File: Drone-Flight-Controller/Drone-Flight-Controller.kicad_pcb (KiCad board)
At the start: 2 copper layers, 30 x 65 mm, 45 parts, among them J1 Screw_Terminal_01x02, J10 TestPoint, J11 TestPoint, J12 TestPoint, J2 Raspberry_Pi_4, J3 TestPoint, J4 TestPoint, J5 TestPoint, J6 TestPoint, J7 TestPoint, J8 TestPoint, J9 TestPoint, SW1 SW_Omron_B3FS, U1 MCP1700x-180xxMB, U2 LMR51430, U3 ADC101C021CIMK, U4 ICM-20948, U5 BMP280, U6 PCA9531PW

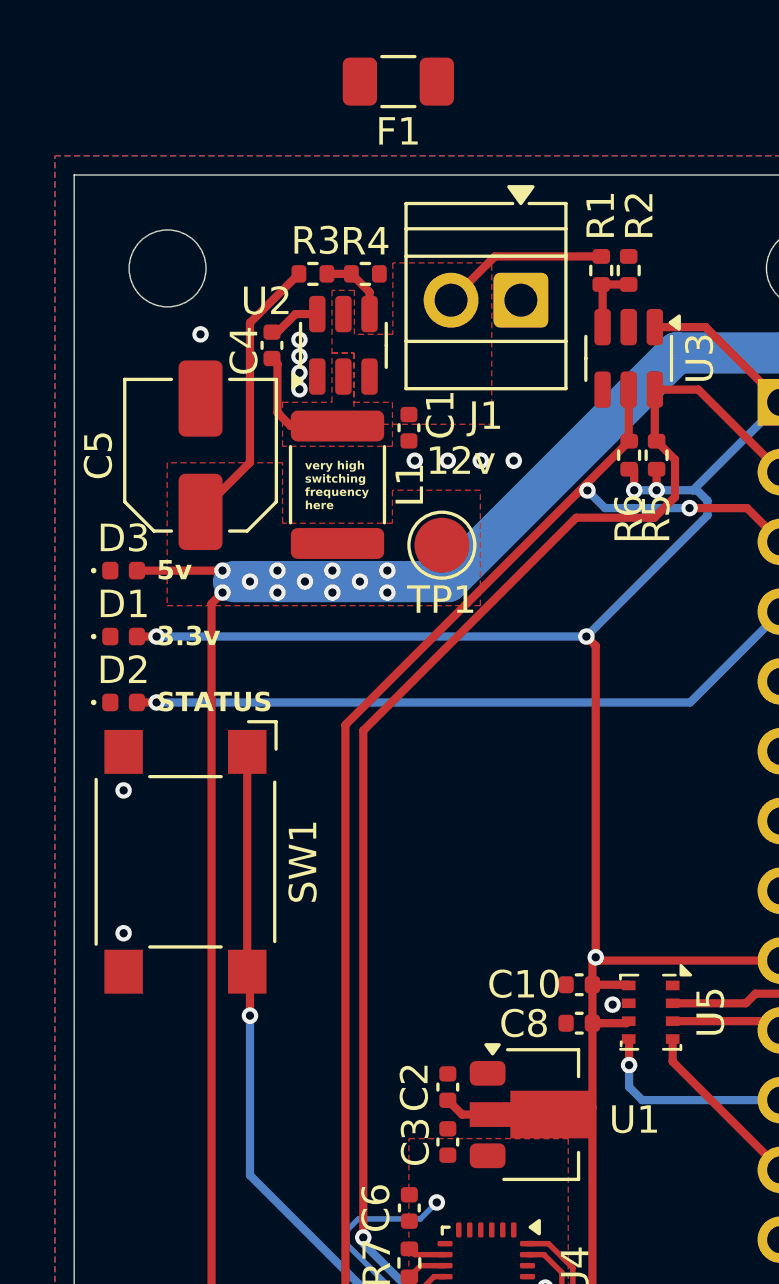
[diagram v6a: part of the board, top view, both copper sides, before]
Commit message: add a fuse
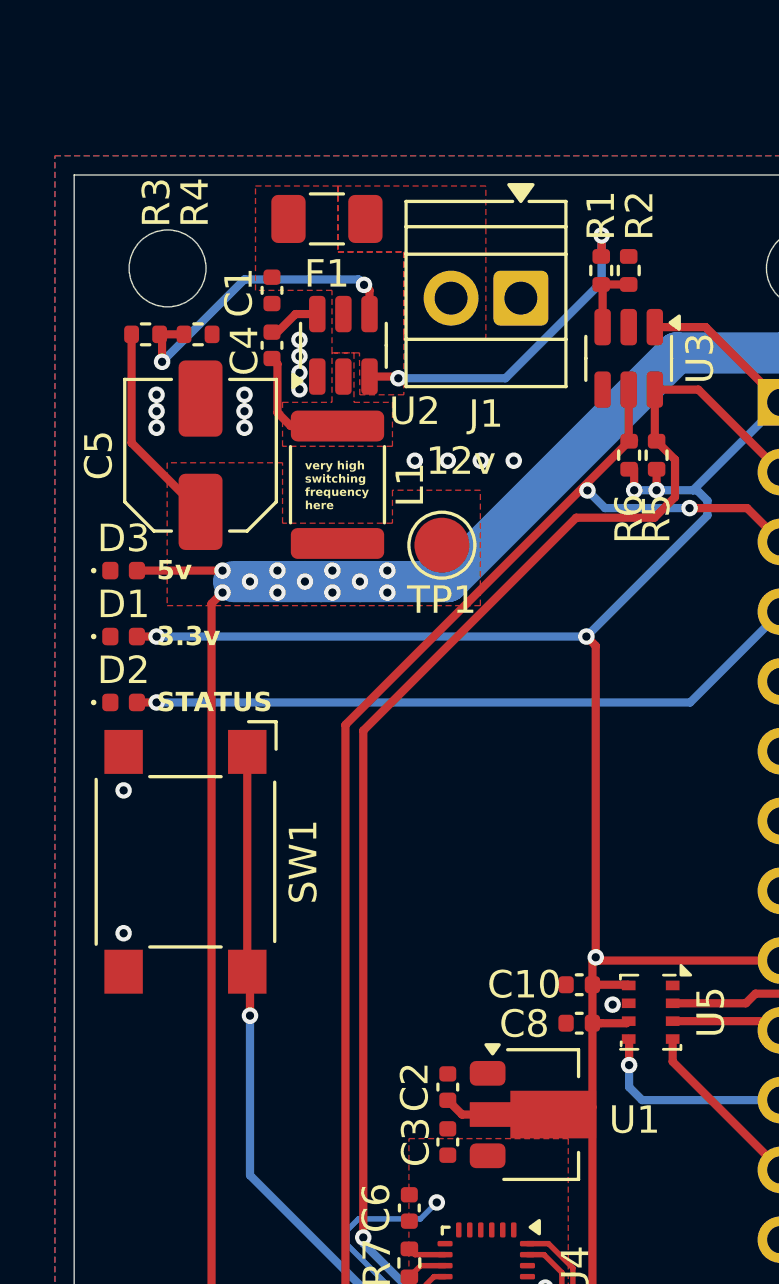
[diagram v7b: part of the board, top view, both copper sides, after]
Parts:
- moved C1 7.06 mm to (19.4, 16.4)
- moved R3 6.48 mm to (14.8, 18.0)
- moved R4 6.48 mm to (16.7, 18.0)
- moved F1 5.64 mm to (21.4, 13.8)
- moved J1 0.07 mm to (28.5, 16.7)
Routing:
- net Net-(U2-FB): track 2.63 -> 11.7 mm, vias 0 -> 2
- net +12V: track 6.12 -> 12.4 mm, vias 0 -> 2
- net +3.3V: track 94.8 -> 90.9 mm
- net +5V: track 75.6 -> 72.9 mm
- net GND: vias 14 -> 19
- added copper zone on F.Cu, net Net-(J1-Pin_2)
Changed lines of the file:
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@@
 	(footprint "TerminalBlock:TerminalBlock_Xinya_XY308-2.54-2P_1x02_P2.54mm_Horizontal"
 		(layer "F.Cu")
-		(at 28.46 16.7575 180)
+		(at 28.46 16.6825 180)
 		(descr "Terminal Block Xinya XY308-2.54-2P, 2 pins, pitch 2.54mm, size 5.58x6.5mm, drill diameter 1.2mm, pad diameter 2mm, http://www.xinyaelectronic.com/product/xy308-254, script-generated using https://gitlab.com/kicad/libraries/kicad-footprint-generator/-/tree/master/scripts/TerminalBlock_Xinya")
 		(tags "THT Terminal Block Xinya XY308-2.54-2P pitch 2.54mm size 5.58x6.5mm drill 1.2mm pad 2mm")
@@
 	(footprint "Fuse:Fuse_1206_3216Metric"
 		(layer "F.Cu")
-		(at 24 8.8 180)
+		(at 21.4 13.8 180)
 		(descr "Fuse SMD 1206 (3216 Metric), square (rectangular) end terminal, IPC-7351 nominal, (Body size source: http://www.tortai-tech.com/upload/download/2011102023233369053.pdf), generated with kicad-footprint-generator")
 		(tags "fuse")
 		(property "Reference" "F1"
-			(at 0 -1.83 0)
+			(at 0 -2 0)
 			(layer "F.SilkS")
 			(effects
@@
 	(footprint "Resistor_SMD:R_0402_1005Metric"
 		(layer "F.Cu")
-		(at 22.8 15.8)
+		(at 16.71 18)
 		(descr "Resistor SMD 0402 (1005 Metric), square (rectangular) end terminal, IPC-7351 nominal, (Body size source: IPC-SM-782 page 72, https://www.pcb-3d.com/wordpress/wp-content/uploads/ipc-sm-782a_amendment_1_and_2.pdf), generated with kicad-footprint-generator")
 		(tags "resistor")
 		(property "Reference" "R4"
-			(at 0 -1.17 0)
+			(at -0.11 -4.8 90)
 			(layer "F.SilkS")
 			(effects
@@
 		(tags "SOT TO_SOT_SMD")
 		(property "Reference" "U2"
-			(at 1.6 -2.8 0)
+			(at -2.4 2.6 0)
 			(layer "F.SilkS")
 			(effects
@@
 	(footprint "Resistor_SMD:R_0402_1005Metric"
 		(layer "F.Cu")
-		(at 20.89 15.8)
+		(at 14.8 18)
 		(descr "Resistor SMD 0402 (1005 Metric), square (rectangular) end terminal, IPC-7351 nominal, (Body size source: IPC-SM-782 page 72, https://www.pcb-3d.com/wordpress/wp-content/uploads/ipc-sm-782a_amendment_1_and_2.pdf), generated with kicad-footprint-generator")
 		(tags "resistor")
 		(property "Reference" "R3"
-			(at 0.11 -1.2 180)
+			(at 0.4 -4.8 270)
 			(layer "F.SilkS")
 			(effects
@@
 	(footprint "Capacitor_SMD:C_0402_1005Metric"
 		(layer "F.Cu")
-		(at 24.385 21.4 -90)
+		(at 19.4 16.4 -90)
 		(descr "Capacitor SMD 0402 (1005 Metric), square (rectangular) end terminal, IPC-7351 nominal, (Body size source: IPC-SM-782 page 76, https://www.pcb-3d.com/wordpress/wp-content/uploads/ipc-sm-782a_amendment_1_and_2.pdf), generated with kicad-footprint-generator")
 		(tags "capacitor")
 		(property "Reference" "C1"
-			(at -0.475 -1.16 90)
+			(at 0.08 1.2 90)
 			(layer "F.SilkS")
 			(effects
@@
 	)
 	(via
-		(at 16.8 18)
+		(at 15.2 20.8)
+		(size 0.6)
+		(drill 0.3)
+		(layers "F.Cu" "B.Cu")
+		(free yes)
+		(net 1)
+	)
+	(via
+		(at 18.4 20.2)
 		(size 0.6)
 		(drill 0.3)
@@
 	)
 	(via
+		(at 18.4 20.8)
+		(size 0.6)
+		(drill 0.3)
+		(layers "F.Cu" "B.Cu")
+		(free yes)
+		(net 1)
+	)
+	(via
 		(at 20.4 18.2)
 		(size 0.6)
@@
 	)
 	(via
+		(at 15.2 21.4)
+		(size 0.6)
+		(drill 0.3)
+		(layers "F.Cu" "B.Cu")
+		(free yes)
+		(net 1)
+	)
+	(via
+		(at 18.4 21.4)
+		(size 0.6)
+		(drill 0.3)
+		(layers "F.Cu" "B.Cu")
+		(free yes)
+		(net 1)
+	)
+	(via
 		(at 27.4 54.8)
 		(size 0.6)
@@
 	)
 	(via
+		(at 15.2 20.2)
+		(size 0.6)
+		(drill 0.3)
+		(layers "F.Cu" "B.Cu")
+		(free yes)
+		(net 1)
+	)
+	(via
 		(at 20.4 19.4)
 		(size 0.6)
@@
 	)
 	(segment
-		(start 30.8 46.4)
-		(end 31.065 46.135)
-		(width 0.3)
-		(layer "F.Cu")
-		(net 2)
-	)
-	(segment
 		(start 31.305 40.795)
 		(end 31.185 40.675)
@@
 	(segment
 		(start 27.3375 46.4)
-		(end 30.8 46.4)
-		(width 0.3)
-		(layer "F.Cu")
-		(net 2)
-	)
-	(segment
-		(start 27.3375 46.4)
 		(end 26.32 46.4)
 		(width 0.3)
@@
 	)
 	(segment
-		(start 16.8 24.4625)
-		(end 18.6 22.6625)
-		(width 0.3)
-		(layer "F.Cu")
-		(net 3)
-	)
-	(segment
 		(start 14.485 26.6)
 		(end 17.6 26.6)
@@
 	)
 	(segment
-		(start 18.6 22.6625)
-		(end 18.6 17.58)
+		(start 14.29 21.9525)
+		(end 16.8 24.4625)
 		(width 0.3)
 		(layer "F.Cu")
@@
 	)
 	(segment
-		(start 17.2 27.8)
-		(end 17.6 27.4)
+		(start 14.29 18)
+		(end 14.29 21.9525)
 		(width 0.3)
 		(layer "F.Cu")
@@
 	)
 	(segment
-		(start 18.6 17.58)
-		(end 20.38 15.8)
+		(start 17.2 27.8)
+		(end 17.6 27.4)
 		(width 0.3)
 		(layer "F.Cu")
@@
 	)
 	(segment
-		(start 31.385 15.165)
-		(end 27.5125 15.165)
+		(start 31.4 15.15)
+		(end 31.385 15.165)
+		(width 0.3)
+		(layer "F.Cu")
+		(net 9)
+	)
+	(segment
+		(start 23.9375 19.5375)
+		(end 22.95 19.5375)
 		(width 0.3)
 		(layer "F.Cu")
@@
 	)
 	(segment
-		(start 27.5125 15.165)
-		(end 25.92 16.7575)
+		(start 31.4 14.4)
+		(end 31.4 15.15)
 		(width 0.3)
 		(layer "F.Cu")
@@
 	)
 	(segment
+		(start 24 19.6)
+		(end 23.9375 19.5375)
+		(width 0.3)
+		(layer "F.Cu")
+		(net 9)
+	)
+	(via
+		(at 31.4 14.4)
+		(size 0.6)
+		(drill 0.3)
+		(layers "F.Cu" "B.Cu")
+		(net 9)
+	)
+	(via
+		(at 24 19.6)
+		(size 0.6)
+		(drill 0.3)
+		(layers "F.Cu" "B.Cu")
+		(net 9)
+	)
+	(segment
+		(start 24 19.6)
+		(end 27.89937 19.6)
+		(width 0.3)
+		(layer "B.Cu")
+		(net 9)
+	)
+	(segment
+		(start 27.89937 19.6)
+		(end 31.4 16.09937)
+		(width 0.3)
+		(layer "B.Cu")
+		(net 9)
+	)
+	(segment
+		(start 31.4 16.09937)
+		(end 31.4 14.4)
+		(width 0.3)
+		(layer "B.Cu")
+		(net 9)
+	)
+	(segment
 		(start 24.3225 68.4)
 		(end 18.11 68.4)
@@
 	)
 	(segment
-		(start 21.4 15.8)
-		(end 22.29 15.8)
+		(start 22.75 16.2)
+		(end 22.95 16.4)
+		(width 0.3)
+		(layer "F.Cu")
+		(net 45)
+	)
+	(segment
+		(start 16.2 18)
+		(end 15.31 18)
 		(width 0.3)
 		(layer "F.Cu")
@@
 	)
 	(segment
-		(start 22.95 16.46)
+		(start 15.4 19)
+		(end 15.4 18.09)
+		(width 0.3)
+		(layer "F.Cu")
+		(net 45)
+	)
+	(segment
+		(start 22.95 16.4)
 		(end 22.95 17.2625)
 		(width 0.3)
@@
 	)
 	(segment
-		(start 22.29 15.8)
-		(end 22.95 16.46)
+		(start 15.4 18.09)
+		(end 15.31 18)
 		(width 0.3)
 		(layer "F.Cu")
 		(net 45)
 	)
+	(via
+		(at 22.75 16.2)
+		(size 0.6)
+		(drill 0.3)
+		(layers "F.Cu" "B.Cu")
+		(net 45)
+	)
+	(via
+		(at 15.4 19)
+		(size 0.6)
+		(drill 0.3)
+		(layers "F.Cu" "B.Cu")
+		(net 45)
+	)
+	(segment
+		(start 22.75 16.2)
+		(end 22.55 16)
+		(width 0.3)
+		(layer "B.Cu")
+		(net 45)
+	)
+	(segment
+		(start 22.55 16)
+		(end 18.4 16)
+		(width 0.3)
+		(layer "B.Cu")
+		(net 45)
+	)
+	(segment
+		(start 18.4 16)
+		(end 15.4 19)
+		(width 0.3)
+		(layer "B.Cu")
+		(net 45)
+	)
 	(segment
 		(start 24.81 51.9)
@@
 	)
 	(zone
-		(net 9)
-		(net_name "+12V")
+		(net 42)
+		(net_name "Net-(U2-SW)")
 		(layer "F.Cu")
 		(hatch edge 0.5)
-		(priority 3)
+		(priority 2)
 		(connect_pads yes
 			(clearance 0)
@@
 		(polygon
 			(pts
-				(xy 23.8 15.4) (xy 23.8 18) (xy 22.4 18) (xy 22.4 16.4) (xy 21.585 16.4) (xy 21.585 18.675) (xy 22.385 18.675)
-				(xy 22.385 21.275) (xy 27.4 21.275) (xy 27.4 15.4)
+				(xy 21.585 18.675) (xy 22.385 18.675) (xy 22.385 20.475) (xy 23.785 20.475) (xy 23.785 22.075) (xy 19.785 22.075)
+				(xy 19.785 20.475) (xy 21.585 20.475)
 			)
 		)
 	)
 	(zone
-		(net 42)
-		(net_name "Net-(U2-SW)")
+		(net 64)
+		(net_name "Net-(J1-Pin_2)")
 		(layer "F.Cu")
 		(hatch edge 0.5)
-		(priority 2)
+		(priority 5)
 		(connect_pads yes
 			(clearance 0)
@@
 		(polygon
 			(pts
-				(xy 21.585 18.675) (xy 22.385 18.675) (xy 22.385 20.475) (xy 23.785 20.475) (xy 23.785 22.075) (xy 19.785 22.075)
-				(xy 19.785 20.475) (xy 21.585 20.475)
+				(xy 21.8 15) (xy 24.2 15) (xy 24.2 18.2) (xy 27.185 18.2) (xy 27.185 12.6) (xy 21.8 12.6)
 			)
 		)
@@
 			)
 		)
+	)
+	(zone
+		(net 9)
+		(net_name "+12V")
+		(layer "F.Cu")
+		(hatch edge 0.5)
+		(priority 3)
+		(connect_pads yes
+			(clearance 0)
+		)
+		(min_thickness 0.25)
+		(filled_areas_thickness no)
+		(fill yes
+			(thermal_gap 0.5)
+			(thermal_bridge_width 0.5)
+		)
+		(polygon
+			(pts
+				(xy 21.8 12.6) (xy 21.8 15) (xy 24.2 15) (xy 24.2 18) (xy 24.2 18) (xy 24.2 20.2) (xy 22.596883 20.2)
+				(xy 22.585 18.675) (xy 21.585 18.675) (xy 21.585 16.4) (xy 18.8 16.4) (xy 18.8 12.6)
+			)
+		)

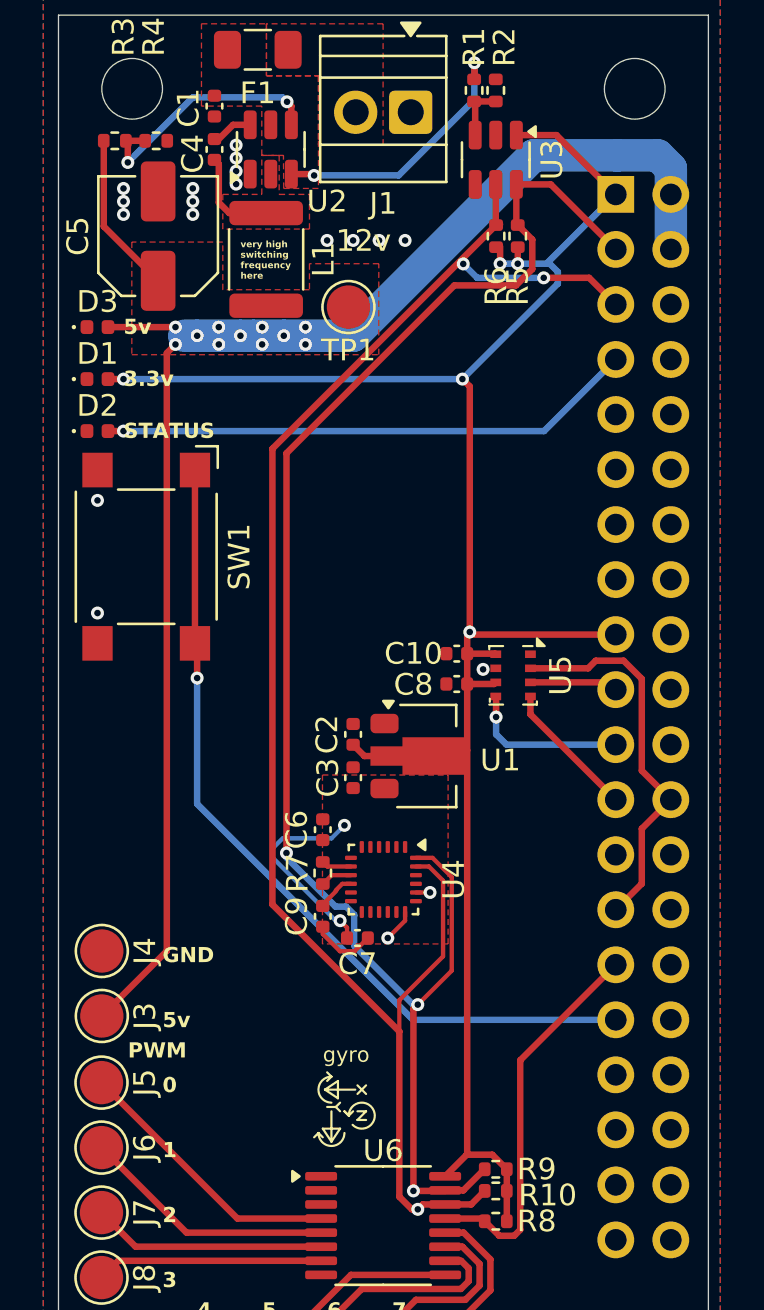
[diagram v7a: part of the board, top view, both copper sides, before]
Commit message: put fuse on pcb
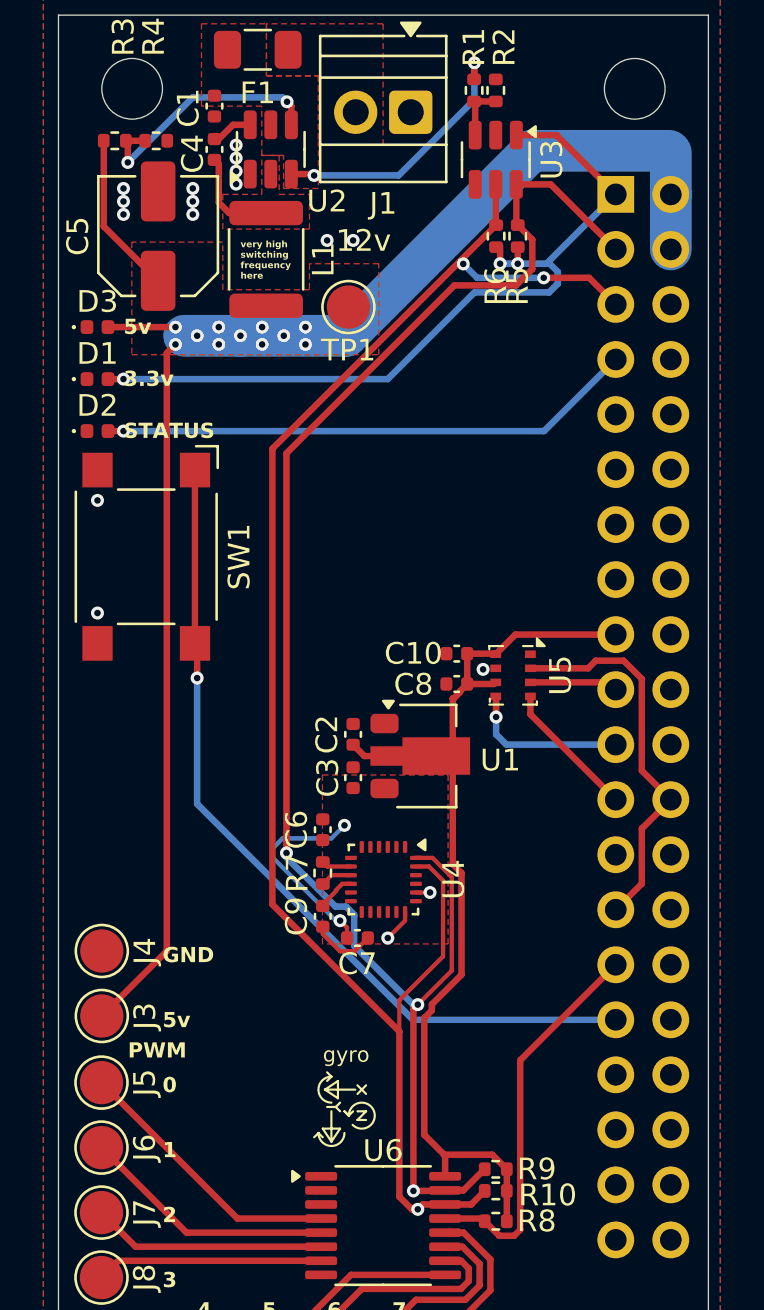
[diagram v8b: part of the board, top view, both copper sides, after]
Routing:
- net +3.3V: track 90.9 -> 79.4 mm, vias 5 -> 3
- net +5V: track 72.9 -> 73.4 mm
- net GND: vias 19 -> 17
